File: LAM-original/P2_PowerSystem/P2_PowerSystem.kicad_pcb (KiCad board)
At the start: 4 copper layers, 115 x 115 mm, 186 parts, among them J1 Conn_02x03_Counter_Clockwise, J10 Conn_01x04_Female, J11 Conn_01x02_Female, J15 Conn_01x05_Female, J2 Conn_02x03_Counter_Clockwise, J21 Conn_01x04_Female, J22 Conn_01x04_Female, J23 Conn_01x04_Female, J3 Conn_02x03_Counter_Clockwise, J37 Conn_02x20_Odd_Even, J38 Conn_02x20_Odd_Even, J39 Conn_01x04_Female, J4 Conn_02x03_Counter_Clockwise, J41 Conn_01x04_Female, J5 Conn_01x02_Female, J6 XT30PW-F, J7 Conn_01x02_Female, J8 Conn_01x04_Female, J9 Conn_01x04_Female, U1 LTC7000EMSE#PBF, U10 MCP601-xOT, U11 74HCT240, U12 SN74HC21-Q1, U13 MCP601-xOT, U14 LM3480-3.3, U15 ACS71240LLCBTR-030B3, U2 LTC7000EMSE#PBF, U3 i3A4W005A150V, U4 Cube_PSM, U5 i3A4W005A150V, U6 i3A4W005A150V, U7 MCP601-xOT, U8 TPS76350, U9 MCP601-xOT

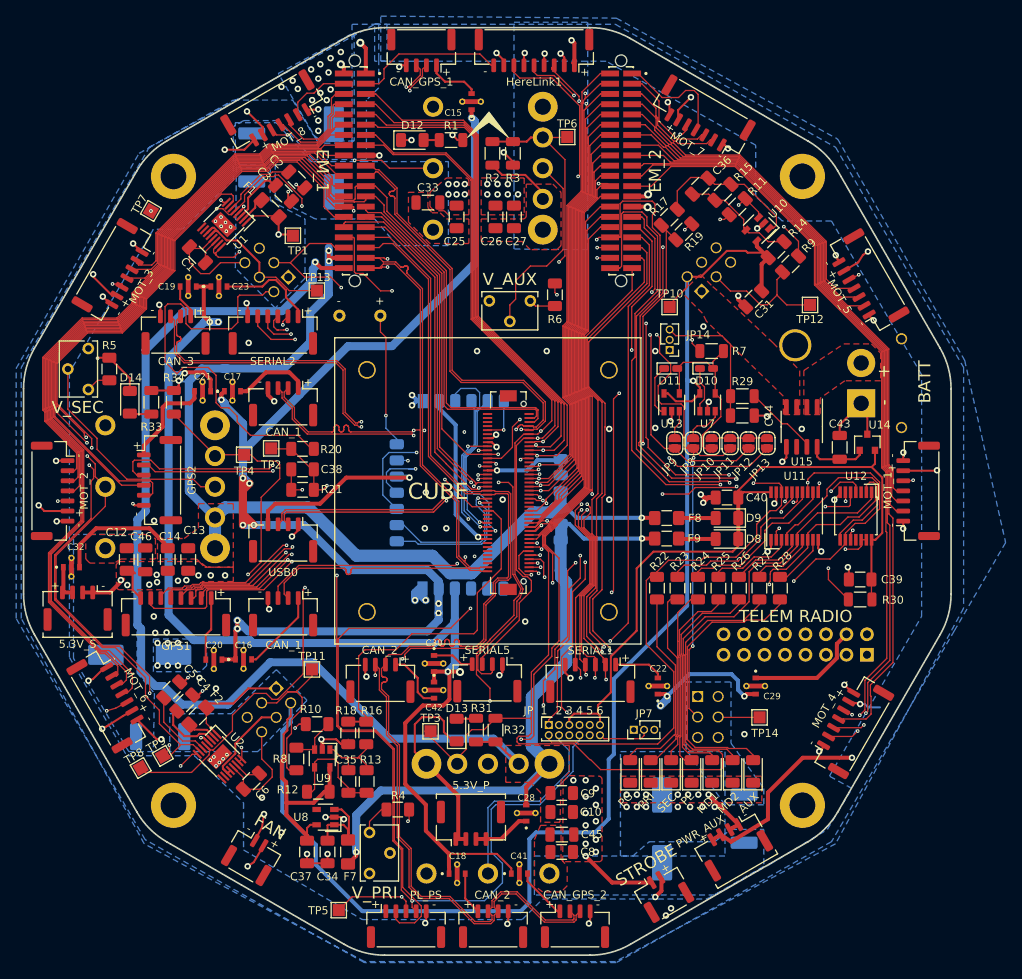
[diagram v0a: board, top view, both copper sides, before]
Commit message: add production files for EasyLAM PDB, STEP for EasySAM
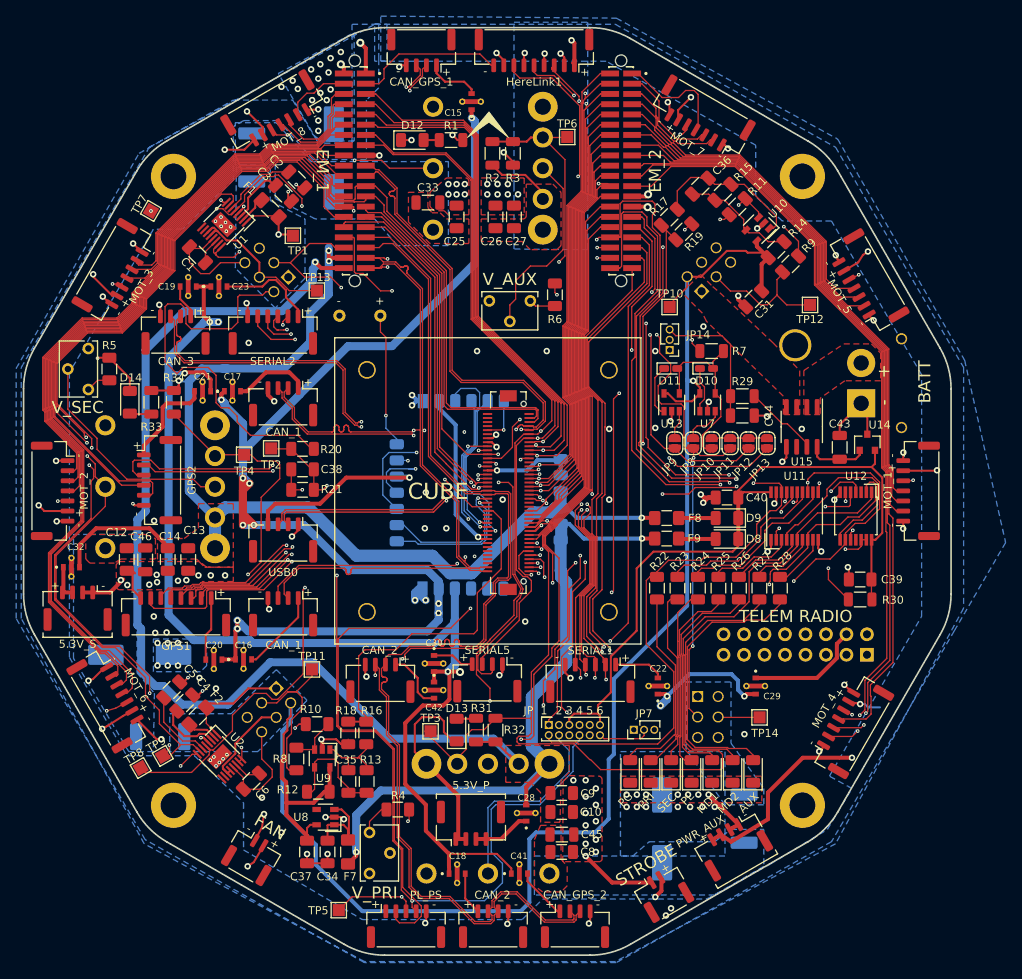
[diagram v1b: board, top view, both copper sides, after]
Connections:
- net FMU-~RESET renamed FMU-~{RESET}
- net ~EXTERN_CS renamed ~{EXTERN_CS}
- net ~FMU-LED_AMBER renamed ~{FMU-LED_AMBER}
- net ~IO-LED_SAFETY_PROT renamed ~{IO-LED_SAFETY_PROT}
- net ~Payload_PW_EN renamed ~{Payload_PW_EN}
- net ~Power_Fault renamed ~{Power_Fault}
- net ~Primary_Power_EN renamed ~{Primary_Power_EN}
- net ~VBUS_VALID renamed ~{VBUS_VALID}
- net ~VDD_5V_PERIPH_EN renamed ~{VDD_5V_PERIPH_EN}
- net ~VDD_5V_PERIPH_OC renamed ~{VDD_5V_PERIPH_OC}
- net ~VDD_BACKUP_VALID renamed ~{VDD_BACKUP_VALID}
- net ~VDD_BRICK_VALID renamed ~{VDD_BRICK_VALID}
- net ~VDD_HIPOWER_OC renamed ~{VDD_HIPOWER_OC}
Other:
- net class 120 ohm JLC PCB (top layer) removed
- net class 90 ohm JLC PCB (top layer) removed
- net class Default removed
- net class Signal (JLC PCB) removed
